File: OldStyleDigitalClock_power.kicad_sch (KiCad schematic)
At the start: 22 parts, among them J1 USB_C_IN, J2 USB_A_OUT, J3 USB_A_OUT, U14 NA555P

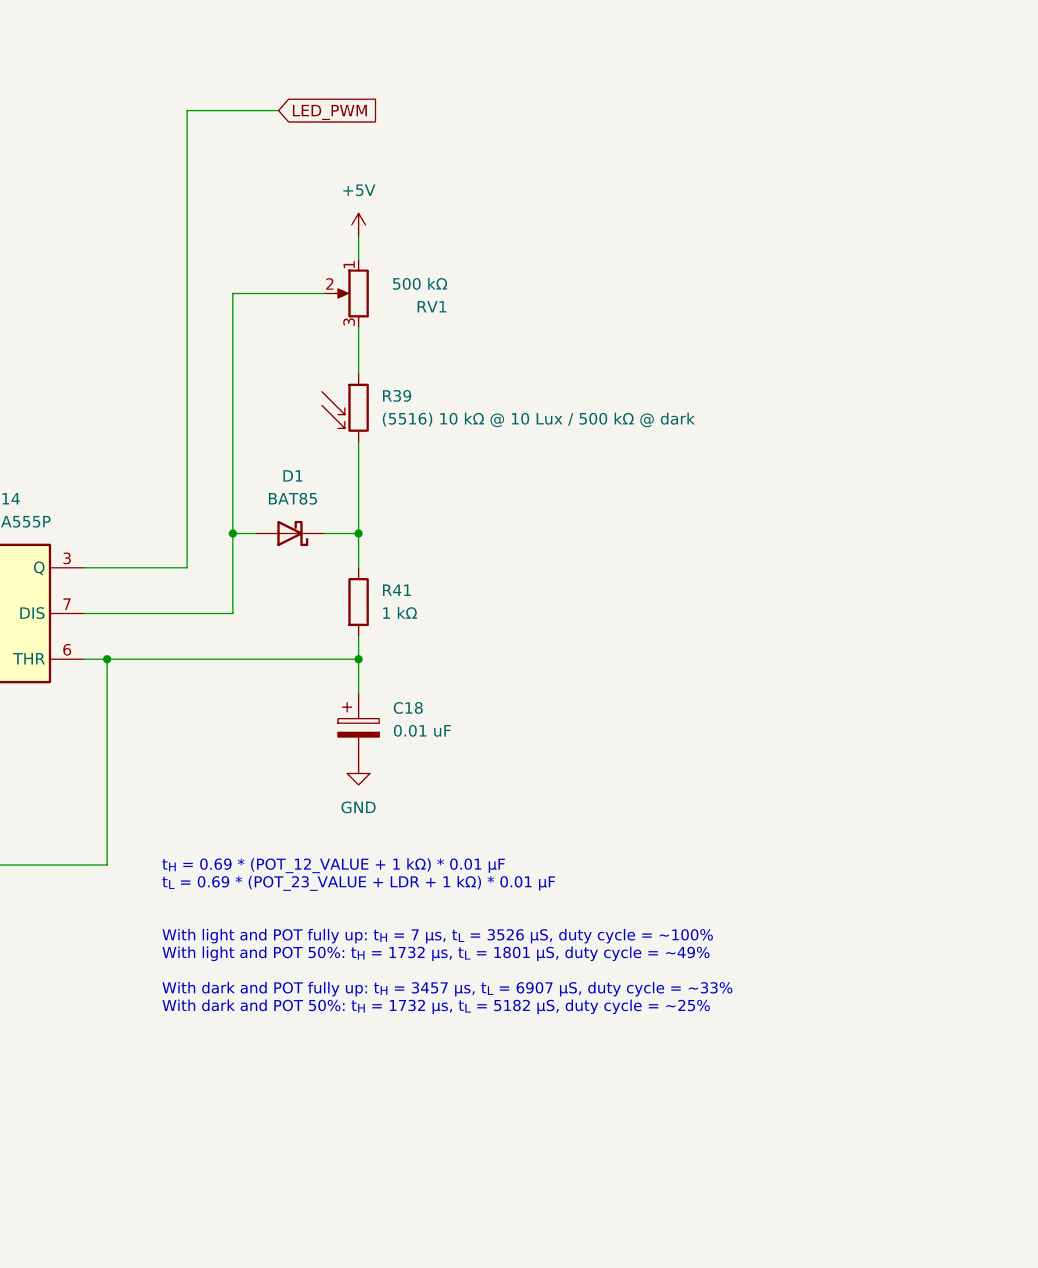
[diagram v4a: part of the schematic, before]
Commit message: New PWM and POT configuration
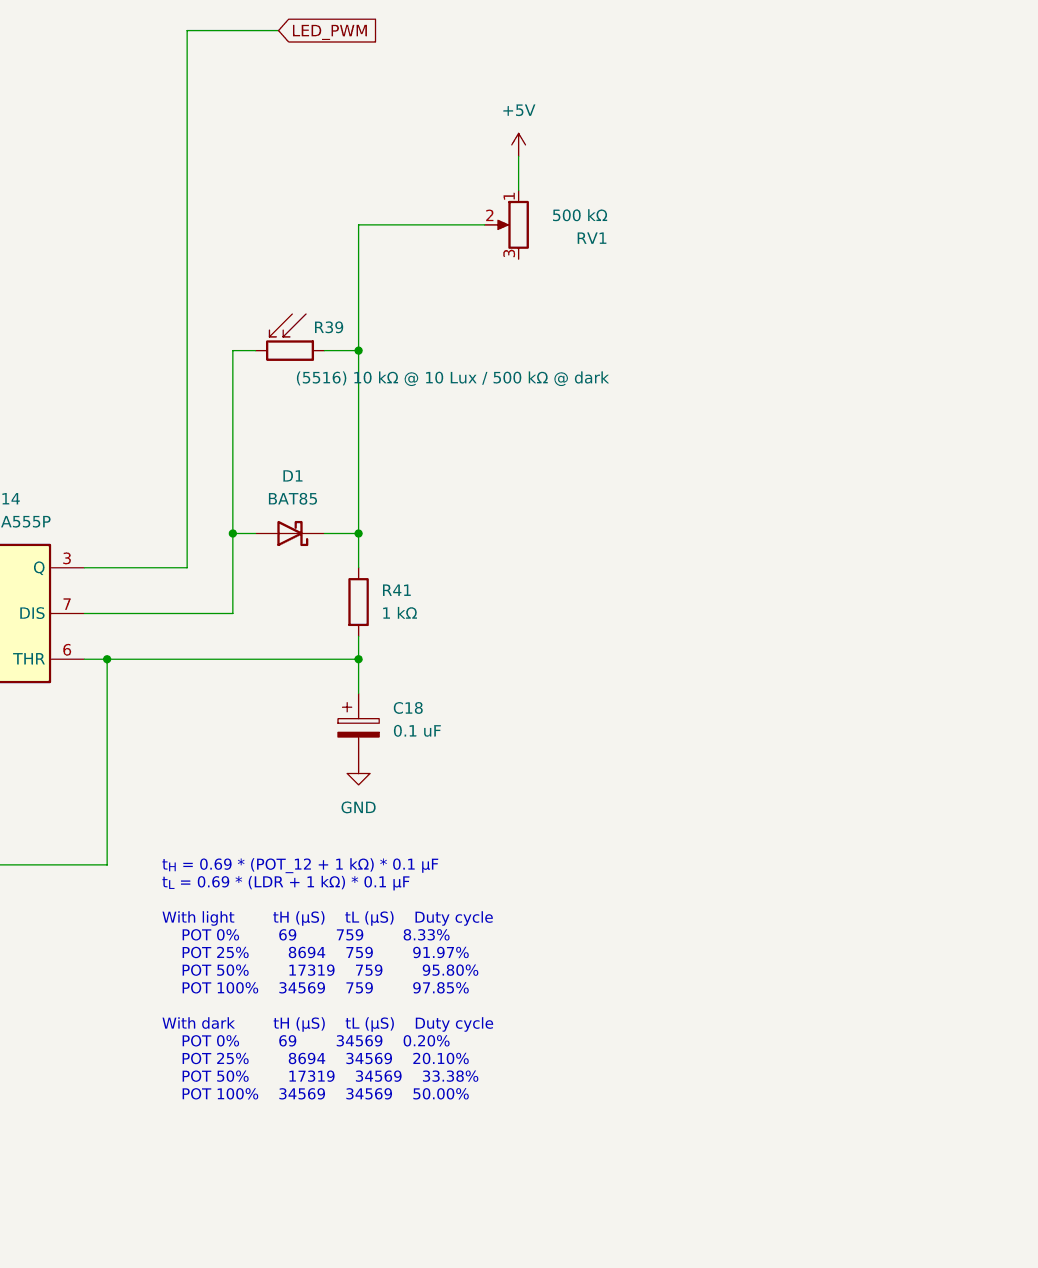
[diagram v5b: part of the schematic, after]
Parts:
- C18: value 0.01 uF -> 0.1 uF
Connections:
- net at D1.2 (A), U14.7 (DIS): now also R39.2; no longer RV1.2
- net at R39.1: now also D1.1 (K), R41.1, RV1.2; no longer RV1.3
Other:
- note added: "t_{H} = 0.69 * (POT_12 + 1 kΩ) * 0.1 µF t_{L} = 0.69 * (LDR + 1 kΩ) * 0.1 µF With light tH (µS) tL (µS) Duty cycle POT 0% 69 759 8.33% POT 25% 8694 759 91.97% POT 50% 17319 759 95.80% POT 100% 34569 759 97.85% With dark tH (µS) tL (µS) Duty cycle POT 0% 69 34569 0.20% POT 25% 8694 34569 20.10% POT 50% 17319 34569 33.38% POT 100% 34569 34569 50.00%"
- note removed: "t_{H} = 0.69 * (POT_12_VALUE + 1 kΩ) * 0.01 µF t_{L} = 0.69 * (POT_23_VALUE + LDR + 1 kΩ) * 0.01 µF With light and POT fully up: t_{H} = 7 µs, t_{L} = 3526 µS, duty cycle = ~100% With light and POT 50%: t_{H} = 1732 µs, t_{L} = 1801 µS, duty cycle = ~49% With dark and POT fully up: t_{H} = 3457 µs, t_{L} = 6907 µS, duty cycle = ~33% With dark and POT 50%: t_{H} = 1732 µs, t_{L} = 5182 µS, duty cy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"
- moved on the sheet: R39, RV1
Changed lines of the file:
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@@
 		(company "Pasquale Lafiosca")
 	)
-	(text "t_{H} = 0.69 * (POT_12_VALUE + 1 kΩ) * 0.01 µF\nt_{L} = 0.69 * (POT_23_VALUE + LDR + 1 kΩ) * 0.01 µF\n\n\nWith light and POT fully up: t_{H} = 7 µs, t_{L} = 3526 µS, duty cycle = ~100%\nWith light and POT 50%: t_{H} = 1732 µs, t_{L} = 1801 µS, duty cycle = ~49%\n\nWith dark and POT fully up: t_{H} = 3457 µs, t_{L} = 6907 µS, duty cycle = ~33%\nWith dark and POT 50%: t_{H} = 1732 µs, t_{L} = 5182 µS, duty cycle = ~25%"
+	(text "t_{H} = 0.69 * (POT_12 + 1 kΩ) * 0.1 µF\nt_{L} = 0.69 * (LDR + 1 kΩ) * 0.1 µF\n\nWith light		tH (µS)	tL (µS)	Duty cycle\n	POT 0%		69		759		8.33%\n	POT 25%		8694	759		91.97%\n	POT 50%		17319	759		95.80%\n	POT 100%	34569	759		97.85%\n				\nWith dark		tH (µS)	tL (µS)	Duty cycle\n	POT 0%		69		34569	0.20%\n	POT 25%		8694	34569	20.10%\n	POT 50%		17319	34569	33.38%\n	POT 100%	34569	34569	50.00%\n\n"
 		(exclude_from_sim no)
 		(at 211.836 111.252 0)
@@
 	)
 	(junction
+		(at 233.68 54.61)
+		(diameter 0)
+		(color 0 0 0 0)
+	)
+	(junction
 		(at 78.74 69.85)
 		(diameter 0)
@@
 	(wire
 		(pts
-			(xy 219.71 48.26) (xy 219.71 74.93)
-		)
-		(stroke
-			(width 0)
-			(type default)
-		)
-	)
-	(wire
-		(pts
 			(xy 40.64 35.56) (xy 41.91 35.56)
 		)
@@
 	(wire
 		(pts
+			(xy 233.68 54.61) (xy 233.68 74.93)
+		)
+		(stroke
+			(width 0)
+			(type default)
+		)
+	)
+	(wire
+		(pts
 			(xy 88.9 69.85) (xy 88.9 80.01)
 		)
@@
 	(wire
 		(pts
-			(xy 233.68 64.77) (xy 233.68 74.93)
-		)
-		(stroke
-			(width 0)
-			(type default)
-		)
-	)
-	(wire
-		(pts
 			(xy 133.35 90.17) (xy 124.46 90.17)
 		)
@@
 	(wire
 		(pts
+			(xy 219.71 54.61) (xy 222.25 54.61)
+		)
+		(stroke
+			(width 0)
+			(type default)
+		)
+	)
+	(wire
+		(pts
 			(xy 115.57 73.66) (xy 115.57 77.47)
 		)
@@
 	(wire
 		(pts
-			(xy 214.63 27.94) (xy 224.79 27.94)
+			(xy 214.63 19.05) (xy 224.79 19.05)
 		)
 		(stroke
@@
 	(wire
 		(pts
-			(xy 214.63 27.94) (xy 214.63 78.74)
+			(xy 214.63 19.05) (xy 214.63 78.74)
 		)
 		(stroke
@@
 	(wire
 		(pts
-			(xy 233.68 41.91) (xy 233.68 44.45)
+			(xy 251.46 33.02) (xy 251.46 36.83)
 		)
 		(stroke
@@
 	(wire
 		(pts
+			(xy 219.71 54.61) (xy 219.71 74.93)
+		)
+		(stroke
+			(width 0)
+			(type default)
+		)
+	)
+	(wire
+		(pts
 			(xy 64.77 87.63) (xy 64.77 109.22)
 		)
@@
 	(wire
 		(pts
-			(xy 233.68 52.07) (xy 233.68 57.15)
-		)
-		(stroke
-			(width 0)
-			(type default)
-		)
-	)
-	(wire
-		(pts
 			(xy 162.56 111.76) (xy 205.74 111.76)
 		)
@@
 	(wire
 		(pts
+			(xy 233.68 40.64) (xy 233.68 54.61)
+		)
+		(stroke
+			(width 0)
+			(type default)
+		)
+	)
+	(wire
+		(pts
 			(xy 214.63 78.74) (xy 203.2 78.74)
 		)
@@
 	(wire
 		(pts
+			(xy 229.87 54.61) (xy 233.68 54.61)
+		)
+		(stroke
+			(width 0)
+			(type default)
+		)
+	)
+	(wire
+		(pts
 			(xy 233.68 88.9) (xy 233.68 86.36)
 		)
@@
 	(wire
 		(pts
-			(xy 219.71 48.26) (xy 229.87 48.26)
+			(xy 233.68 40.64) (xy 247.65 40.64)
 		)
 		(stroke
@@
 	(global_label "LED_PWM"
 		(shape input)
-		(at 224.79 27.94 0)
+		(at 224.79 19.05 0)
 		(fields_autoplaced yes)
 		(effects
@@
 		)
 		(property "Intersheetrefs" "${INTERSHEET_REFS}"
-			(at 236.3627 27.94 0)
+			(at 236.3627 19.05 0)
 			(effects
 				(font
@@
 			)
 		)
-		(property "Value" "0.01 uF"
+		(property "Value" "0.1 uF"
 			(at 237.49 96.9009 0)
 			(effects
@@
 	(symbol
 		(lib_id "Device:R_Potentiometer")
-		(at 233.68 48.26 0)
+		(at 251.46 40.64 0)
 		(mirror y)
 		(unit 1)
@@
 		(dnp no)
 		(property "Reference" "RV1"
-			(at 243.586 49.784 0)
+			(at 261.366 42.164 0)
 			(effects
 				(font
@@
 		)
 		(property "Value" "500 kΩ"
-			(at 243.586 47.244 0)
+			(at 261.366 39.624 0)
 			(effects
 				(font
@@
 		)
 		(property "Footprint" ""
-			(at 233.68 48.26 0)
+			(at 251.46 40.64 0)
 			(effects
 				(font
@@
 		)
 		(property "Datasheet" "~"
-			(at 233.68 48.26 0)
+			(at 251.46 40.64 0)
 			(effects
 				(font
@@
 		)
 		(property "Description" "Potentiometer"
-			(at 233.68 48.26 0)
+			(at 251.46 40.64 0)
 			(effects
 				(font
@@
 	(symbol
 		(lib_id "power:VDD")
-		(at 233.68 41.91 0)
+		(at 251.46 33.02 0)
 		(unit 1)
 		(exclude_from_sim no)
@@
 		(dnp no)
 		(property "Reference" "#PWR063"
-			(at 233.68 45.72 0)
+			(at 251.46 36.83 0)
 			(effects
 				(font
@@
 		)
 		(property "Value" "+5V"
-			(at 233.68 36.83 0)
+			(at 251.46 27.94 0)
 			(effects
 				(font
@@
 		)
 		(property "Footprint" ""
-			(at 233.68 41.91 0)
+			(at 251.46 33.02 0)
 			(effects
 				(font
@@
 		)
 		(property "Datasheet" ""
-			(at 233.68 41.91 0)
+			(at 251.46 33.02 0)
 			(effects
 				(font
@@
 		)
 		(property "Description" ""
-			(at 233.68 41.91 0)
+			(at 251.46 33.02 0)
 			(effects
 				(font
@@
 	(symbol
 		(lib_id "Device:R_Photo")
-		(at 233.68 60.96 0)
+		(at 226.06 54.61 270)
 		(unit 1)
 		(exclude_from_sim no)
@@
 		(on_board yes)
 		(dnp no)
-		(fields_autoplaced yes)
 		(property "Reference" "R39"
-			(at 236.22 59.6899 0)
-			(effects
-				(font
-					(size 1.27 1.27)
-				)
-				(justify left)
+			(at 230.378 52.07 90)
+			(effects
+				(font
+					(size 1.27 1.27)
+				)
 			)
 		)
 		(property "Value" "(5516) 10 kΩ @ 10 Lux / 500 kΩ @ dark"
-			(at 236.22 62.2299 0)
-			(effects
-				(font
-					(size 1.27 1.27)
-				)
-				(justify left)
+			(at 244.094 57.658 90)
+			(effects
+				(font
+					(size 1.27 1.27)
+				)
 			)
 		)
 		(property "Footprint" ""
-			(at 234.95 67.31 90)
+			(at 219.71 55.88 90)
 			(effects
 				(font
@@
 		)
 		(property "Datasheet" "~"
-			(at 233.68 62.23 0)
+			(at 224.79 54.61 0)
 			(effects
 				(font
@@
 		)
 		(property "Description" "Photoresistor"
-			(at 233.68 60.96 0)
-			(effects
-				(font
+			(at 226.06 54.61 0)
+			(effects
+				(font

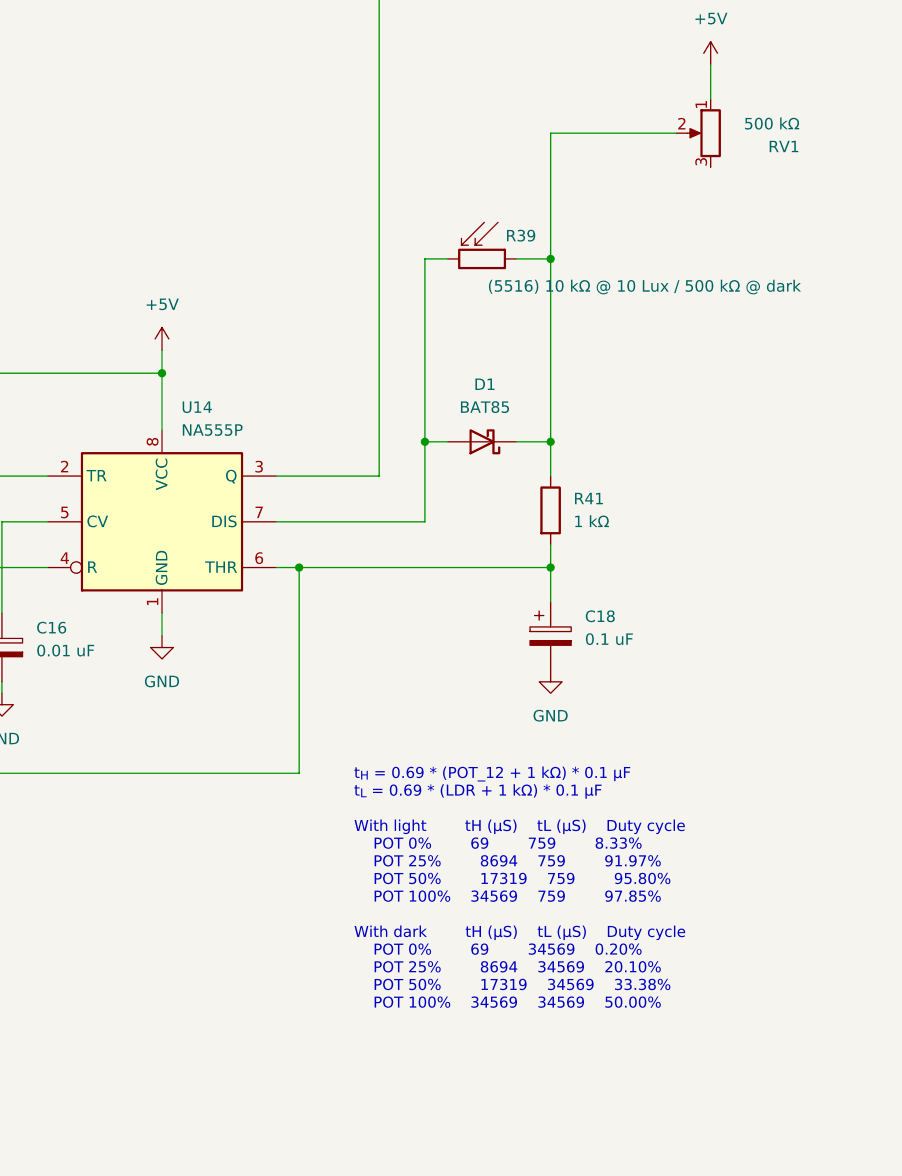
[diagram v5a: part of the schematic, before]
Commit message: Added pull up on NA555 output. Minor changes.
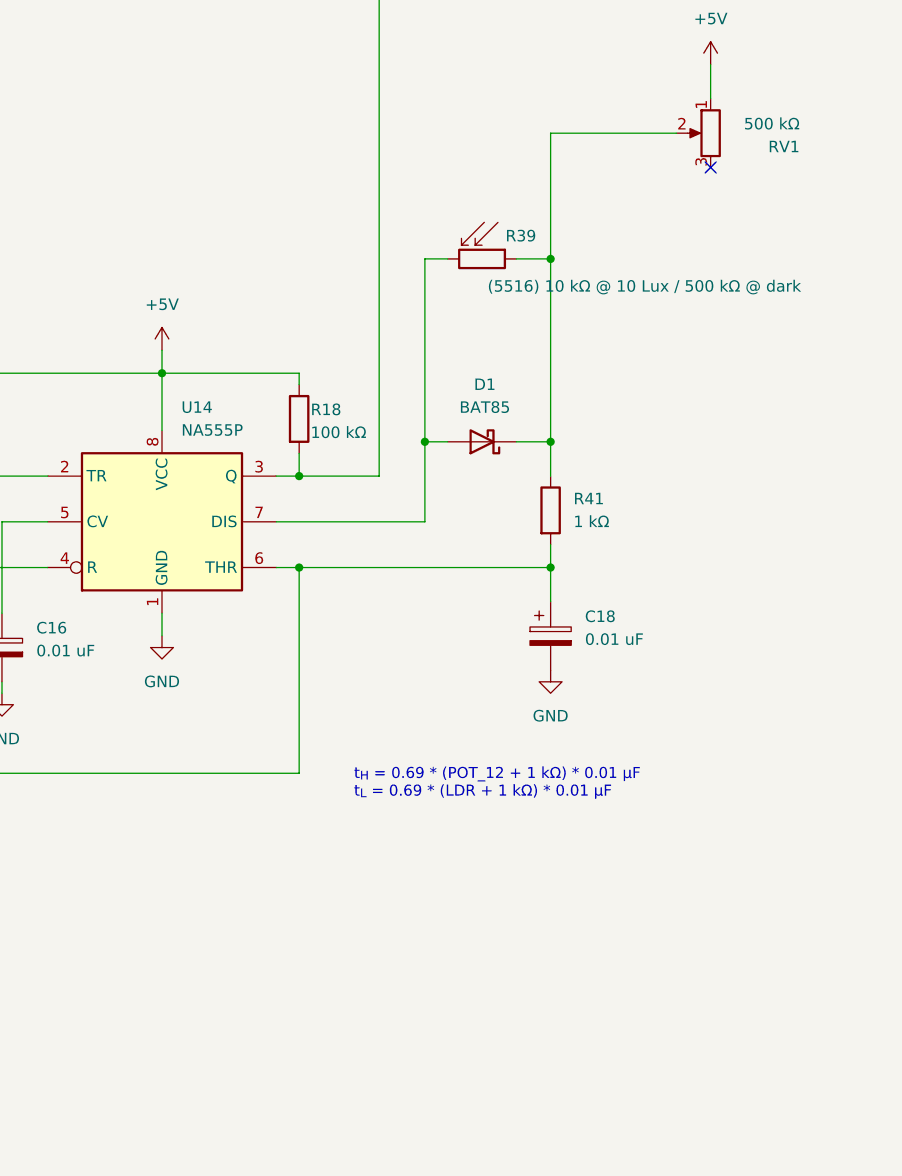
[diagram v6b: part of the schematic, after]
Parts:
- added R18: 100 kΩ, symbol Device:R
- C18: value 0.1 uF -> 0.01 uF
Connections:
- net +5V: now also R18.1
- net LED_PWM: now also R18.2
- no-connect marks 2 -> 3
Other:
- note added: "t_{H} = 0.69 * (POT_12 + 1 kΩ) * 0.01 µF t_{L} = 0.69 * (LDR + 1 kΩ) * 0.01 µF"
- note removed: "t_{H} = 0.69 * (POT_12 + 1 kΩ) * 0.1 µF t_{L} = 0.69 * (LDR + 1 kΩ) * 0.1 µF With light tH (µS) tL (µS) Duty cycle POT 0% 69 759 8.33% POT 25% 8694 759 91.97% POT 50% 17319 759 95.80% POT 100% 34569 759 97.85% With dark tH (µS) tL (µS) Duty cycle POT 0% 69 34569 0.20% POT 25% 8694 34569 20.10% POT 50% 17319 34569 33.38% POT 100% 34569 34569 50.00%"
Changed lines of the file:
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@@
 		(company "Pasquale Lafiosca")
 	)
-	(text "t_{H} = 0.69 * (POT_12 + 1 kΩ) * 0.1 µF\nt_{L} = 0.69 * (LDR + 1 kΩ) * 0.1 µF\n\nWith light		tH (µS)	tL (µS)	Duty cycle\n	POT 0%		69		759		8.33%\n	POT 25%		8694	759		91.97%\n	POT 50%		17319	759		95.80%\n	POT 100%	34569	759		97.85%\n				\nWith dark		tH (µS)	tL (µS)	Duty cycle\n	POT 0%		69		34569	0.20%\n	POT 25%		8694	34569	20.10%\n	POT 50%		17319	34569	33.38%\n	POT 100%	34569	34569	50.00%\n\n"
+	(text "t_{H} = 0.69 * (POT_12 + 1 kΩ) * 0.01 µF\nt_{L} = 0.69 * (LDR + 1 kΩ) * 0.01 µF\n\n"
 		(exclude_from_sim no)
 		(at 211.836 111.252 0)
@@
 	)
 	(junction
+		(at 205.74 78.74)
+		(diameter 0)
+		(color 0 0 0 0)
+	)
+	(junction
 		(at 33.02 50.8)
 		(diameter 0)
@@
 	)
 	(no_connect
+		(at 251.46 44.45)
+	)
+	(no_connect
 		(at 54.61 97.79)
 	)
@@
 	(wire
 		(pts
+			(xy 190.5 67.31) (xy 205.74 67.31)
+		)
+		(stroke
+			(width 0)
+			(type default)
+		)
+	)
+	(wire
+		(pts
 			(xy 124.46 90.17) (xy 115.57 90.17)
 		)
@@
 	(wire
 		(pts
+			(xy 205.74 76.2) (xy 205.74 78.74)
+		)
+		(stroke
+			(width 0)
+			(type default)
+		)
+	)
+	(wire
+		(pts
 			(xy 172.72 83.82) (xy 177.8 83.82)
 		)
@@
 	(wire
 		(pts
+			(xy 205.74 68.58) (xy 205.74 67.31)
+		)
+		(stroke
+			(width 0)
+			(type default)
+		)
+	)
+	(wire
+		(pts
 			(xy 172.72 93.98) (xy 172.72 83.82)
 		)
@@
 	(wire
 		(pts
+			(xy 205.74 78.74) (xy 203.2 78.74)
+		)
+		(stroke
+			(width 0)
+			(type default)
+		)
+	)
+	(wire
+		(pts
 			(xy 53.34 50.8) (xy 53.34 53.34)
 		)
@@
 	(wire
 		(pts
-			(xy 214.63 78.74) (xy 203.2 78.74)
+			(xy 214.63 78.74) (xy 205.74 78.74)
 		)
 		(stroke
@@
 			)
 		)
-		(property "Value" "0.1 uF"
+		(property "Value" "0.01 uF"
 			(at 237.49 96.9009 0)
 			(effects
@@
 					(unit 1)
 				)
+			)
+		)
+	)
+	(symbol
+		(lib_id "Device:R")
+		(at 205.74 72.39 0)
+		(unit 1)
+		(exclude_from_sim no)
+		(in_bom yes)
+		(on_board yes)
+		(dnp no)
+		(property "Reference" "R18"
+			(at 207.01 71.374 0)
+			(effects
+				(font
+					(size 1.27 1.27)
+				)
+				(justify left)
+			)
+		)
+		(property "Value" "100 kΩ"
+			(at 207.01 73.914 0)
+			(effects
+				(font
+					(size 1.27 1.27)
+				)
+				(justify left)
+			)
+		)
+		(property "Footprint" ""
+			(at 203.962 72.39 90)
+			(effects
+				(font
+					(size 1.27 1.27)
+				)
+				(hide yes)
+			)
+		)
+		(property "Datasheet" "~"
+			(at 205.74 72.39 0)
+			(effects
+				(font
+					(size 1.27 1.27)
+				)
+				(hide yes)
+			)
+		)
+		(property "Description" "Resistor"
+			(at 205.74 72.39 0)
+			(effects
+				(font
+					(size 1.27 1.27)
+				)
+				(hide yes)
+			)
+		)
+		(pin "2"
+		)
+		(pin "1"
+		)
+		(instances
+			(project "OldStyleDigitalClock"
+				(path "/a24f1d5b-eb61-47a3-9a92-6515e74f7a21/31b03831-3d01-49ef-8f86-173fa6c5d953"
+					(reference "R18")
+					(unit 1)
+				)
